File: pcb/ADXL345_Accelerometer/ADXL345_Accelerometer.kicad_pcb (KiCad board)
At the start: 2 copper layers, 25.4 x 22.9 mm, 18 parts, among them J1 Conn_01x09, Q1 BSS138, Q2 BSS138, U1 ADXL345BCCZ, U2 AP2112K-3.3

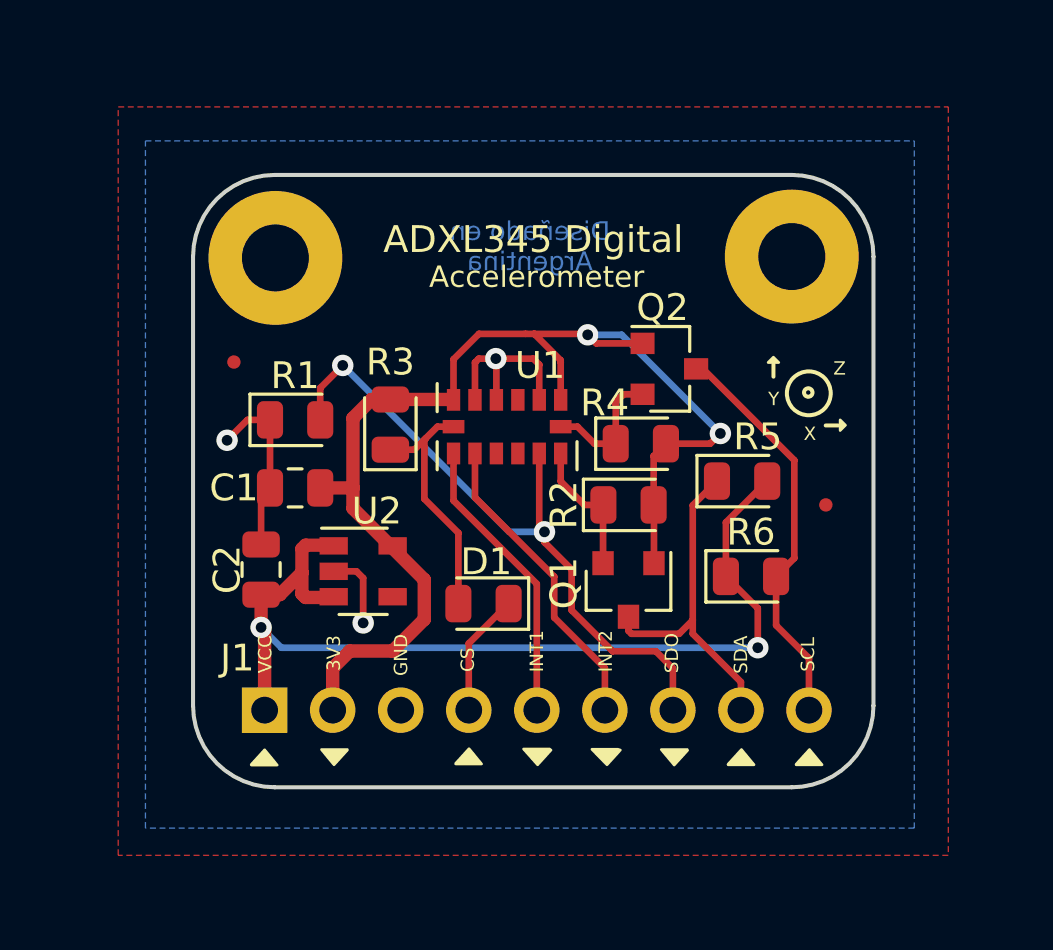
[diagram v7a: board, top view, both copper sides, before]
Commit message: Correcciones
Se corrigio de acuerdo a las ultimas recomendaciones realizadas por el docente.
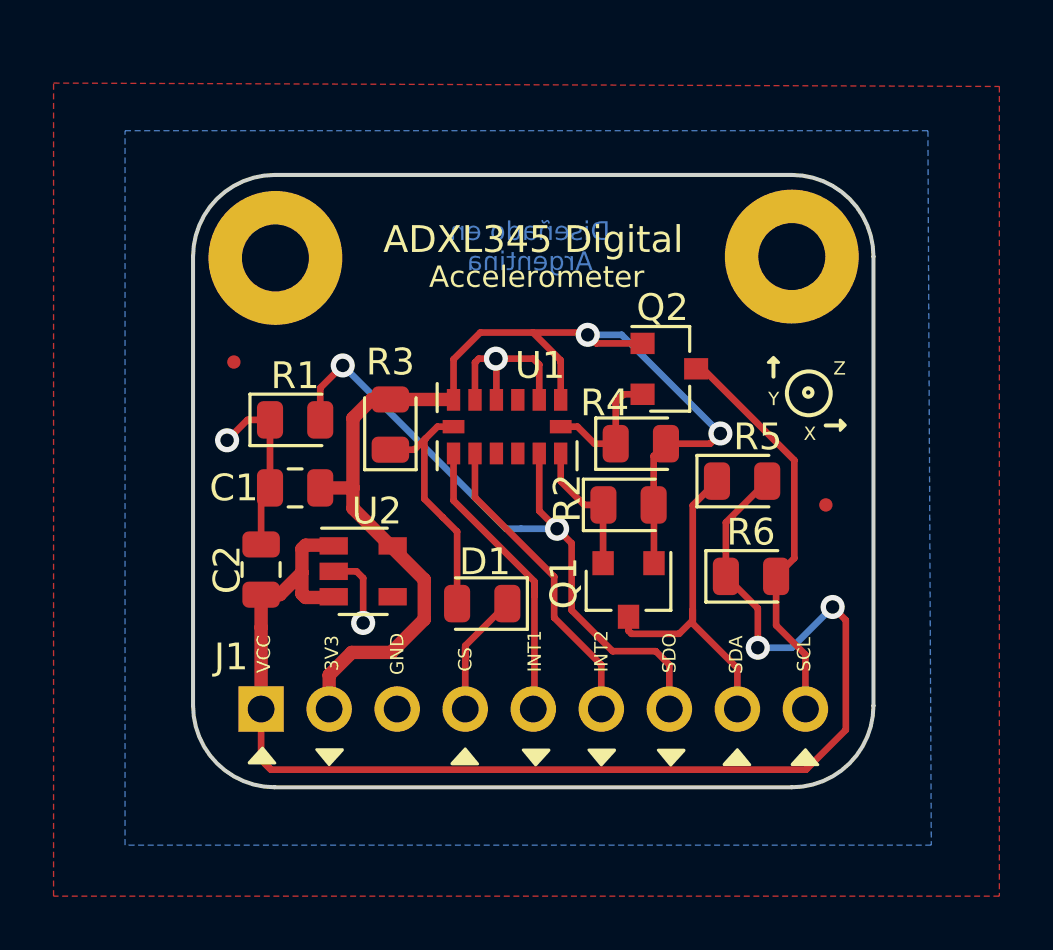
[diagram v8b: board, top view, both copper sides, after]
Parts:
- moved J1 0.14 mm to (133.9, 101.2)
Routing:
- net VCC: track 36.6 -> 50.8 mm
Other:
- board text added: "Fabricante MEYER SA Estándares de fabricación Diámetro de agujero: 16 (0,40 mm) Diámetro de pad o vía: 28 (0,70 mm) Ancho de traza: 5 (0,125 mm) Separación entre trazas; 5 (0,125 mm) Separación entre traza y pad/vía: 5 (0,125 mm) Distancia de cobre a borde: 12 (0,30 mm) Antisoldante: 2 (0.05 mm) Altura - trazo de letras: 30 - 5"
- board text added: "Grilla: 0,1 mm Ancho de las pistas: 0,25 mm Vias: 0.9/0.5mm Pistas: 0.25mm, 0.5mm Margen: 0.40 mm Terminación: HASL"
- board text removed: "Grilla: 0,5 mm Ancho de las pistas: 0,25 mm Via: 0,80 mm ( 0,40 mm ) Margen: 0.40 mm Terminación: HASL"
